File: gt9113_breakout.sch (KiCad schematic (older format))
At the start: 54 parts, among them J1 Conn_01x04_Male, J2 10118194-0001LF, J3 Conn_01x04_Male, J4 Conn_01x07_Male, J5 Conn_01x01_Male, J7 504740-5100, J8 504740-5100, Q1 2N7002E, U1 mXT2952TD, U2 HT7533-1-SOT89, Y1 DNF/16MHz

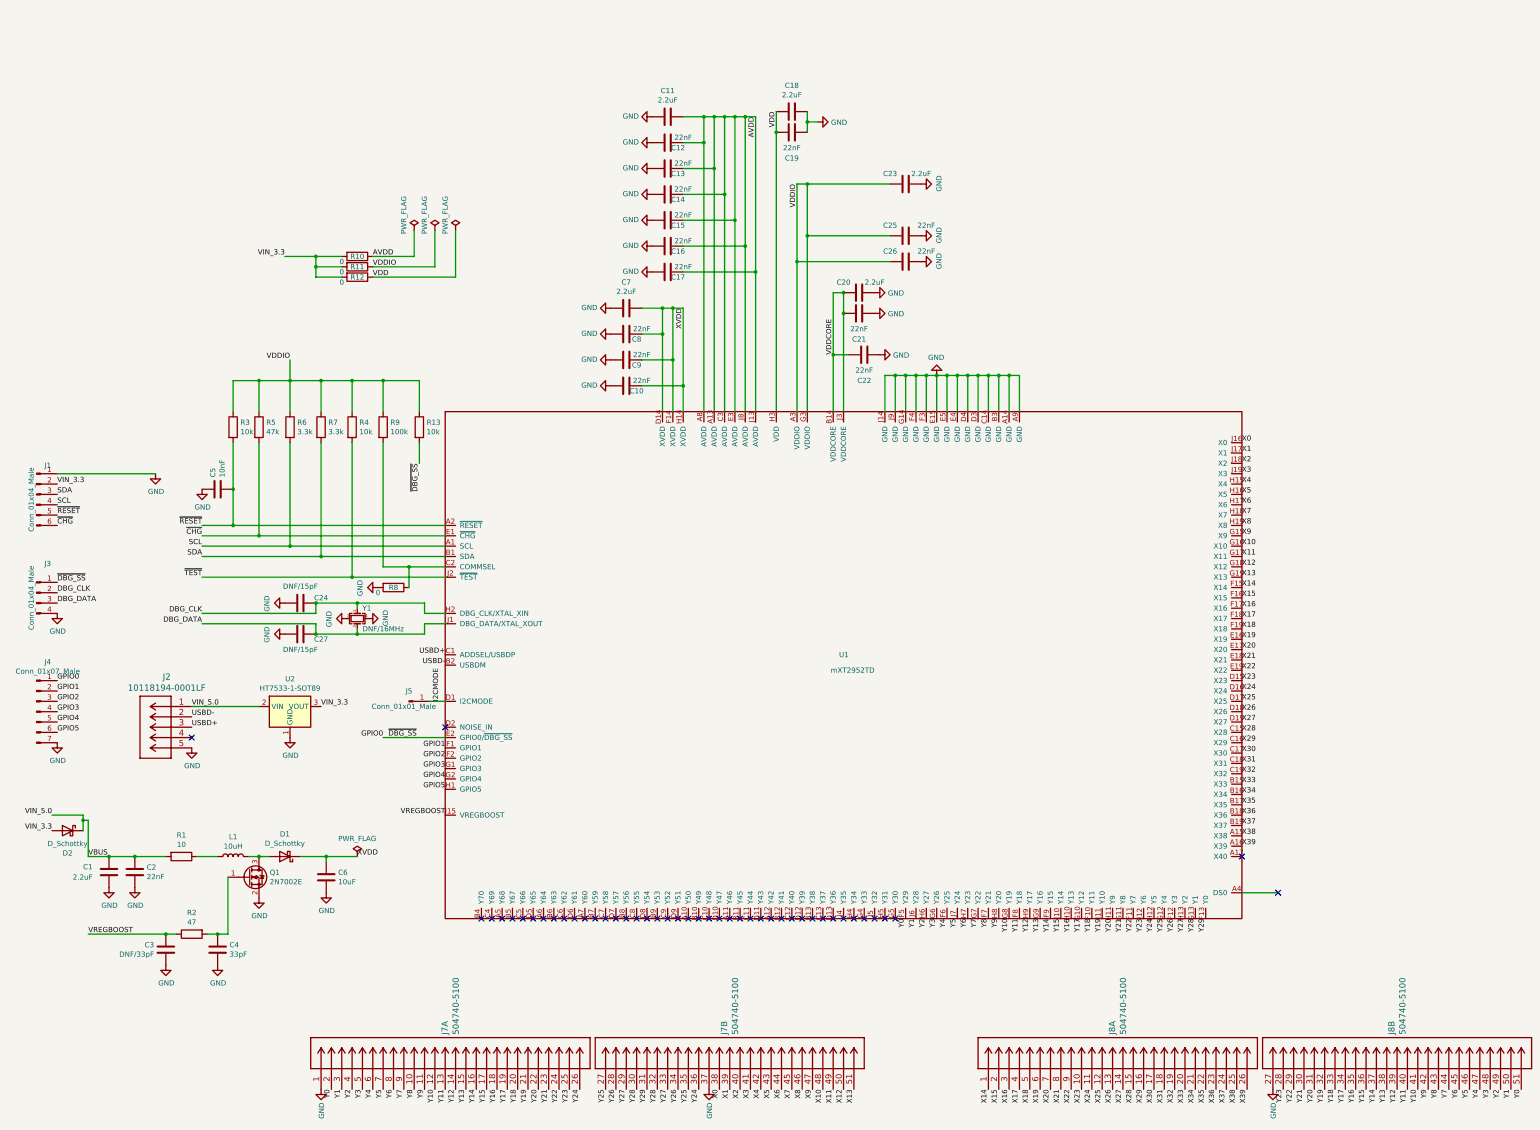
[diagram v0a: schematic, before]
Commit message: Remove all traces of atmxt2952. enable pth_and_npth_single_file since that's what jlcpcb wants
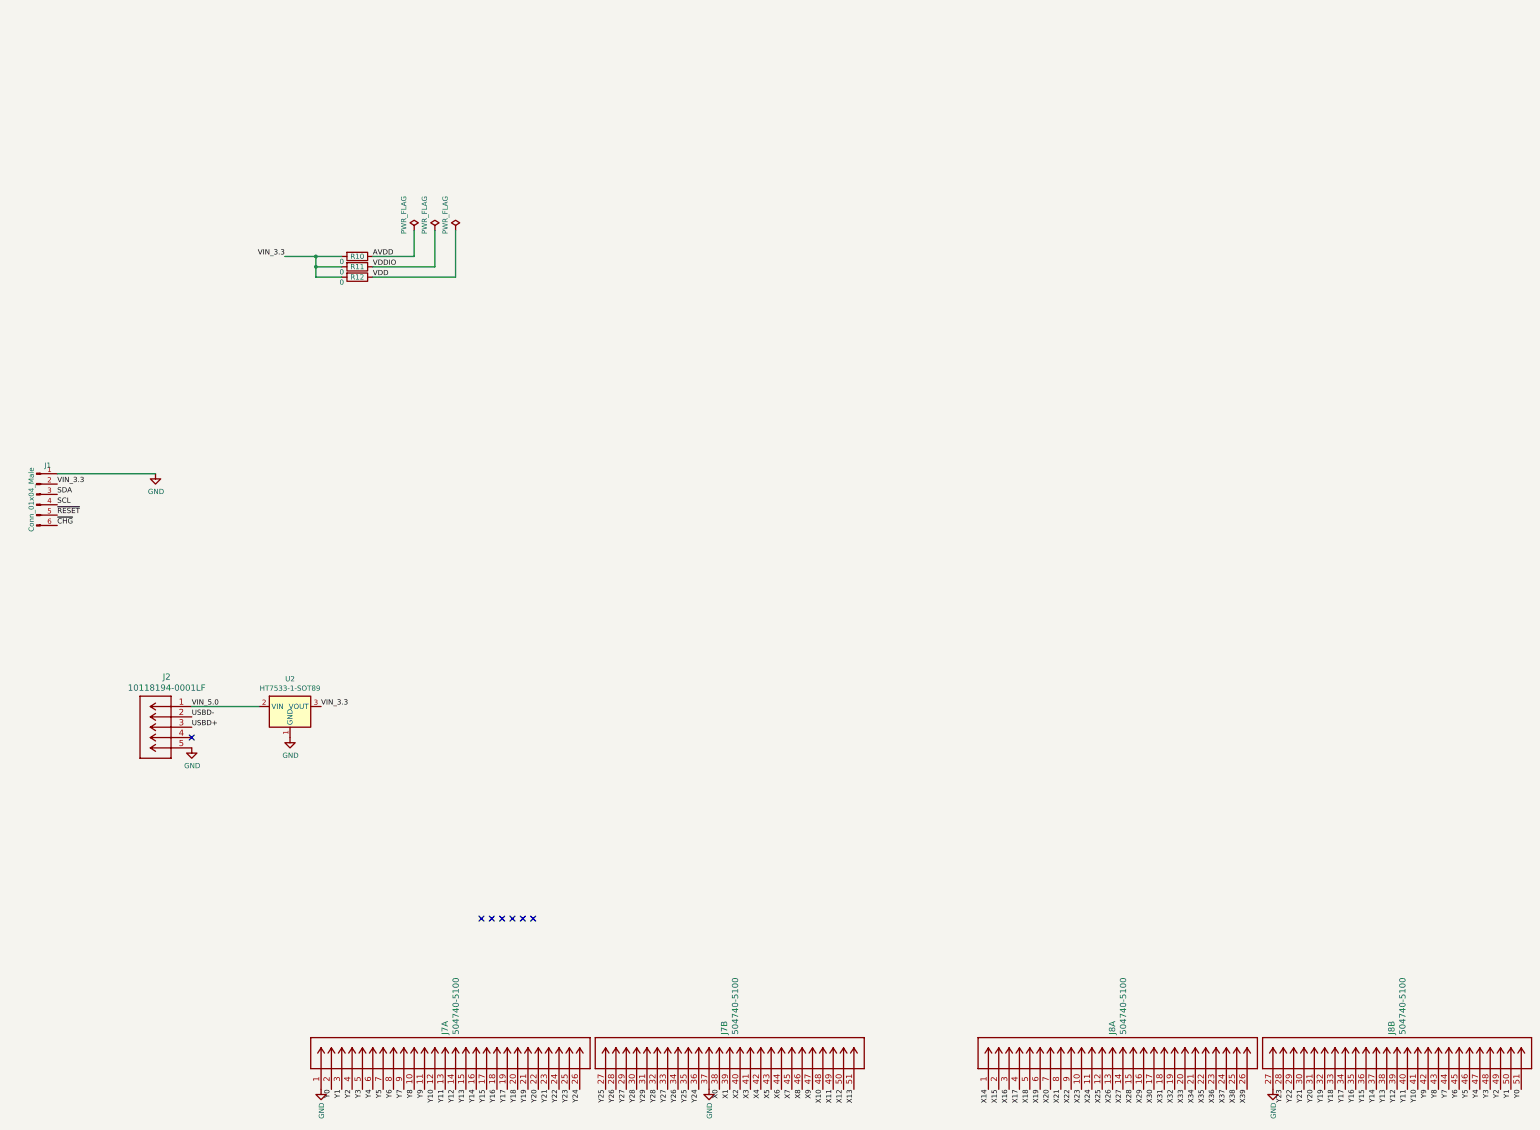
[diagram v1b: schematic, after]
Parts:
- removed C1, C11, C18, C20, C23, C7: 2.2uF, Capacitor_SMD:C_0603_1608Metric, symbol Device:C
- removed C10, C12, C13, C14, C15, C16, C17, C19, C2, C21, C22, C25, C26, C8, C9: 22nF, Capacitor_SMD:C_0402_1005Metric, symbol Device:C
- removed C24, C27: DNF/15pF, Capacitor_SMD:C_0603_1608Metric_Pad1.05x0.95mm_HandSolder, symbol Device:C
- removed C3: DNF/33pF, Capacitor_SMD:C_0603_1608Metric_Pad1.05x0.95mm_HandSolder, symbol Device:C
- removed C4: 33pF, Capacitor_SMD:C_0402_1005Metric, symbol Device:C
- removed C5: 10nF, Capacitor_SMD:C_0402_1005Metric, symbol Device:C
- removed C6: 10uF, Capacitor_SMD:C_0603_1608Metric, symbol Device:C
- removed D1, D2: D_Schottky, Diode_SMD:D_SOD-123, symbol Device:D_Schottky
- removed J3: Conn_01x04_Male, Connector_PinHeader_1.00mm:PinHeader_1x04_P1.00mm_Vertical, symbol Connector:Conn_01x04_Male
- removed J4: Conn_01x07_Male, Connector_PinHeader_1.00mm:PinHeader_1x07_P1.00mm_Vertical, symbol Connector:Conn_01x07_Male
- removed J5: Conn_01x01_Male, Connector_PinHeader_1.00mm:PinHeader_1x01_P1.00mm_Vertical, symbol Connector:Conn_01x01_Male
- removed L1: 10uH, Inductor_SMD:L_0603_1608Metric, symbol Device:L
- removed Q1: 2N7002E, Package_TO_SOT_SMD:SOT-23, symbol Transistor_FET:2N7002E
- removed R1: 10, Resistor_SMD:R_0402_1005Metric, symbol Device:R
- removed R13, R3, R4: 10k, Resistor_SMD:R_0402_1005Metric, symbol Device:R
- removed R2: 47, Resistor_SMD:R_0402_1005Metric, symbol Device:R
- removed R5: 47k, Resistor_SMD:R_0402_1005Metric, symbol Device:R
- removed R6, R7: 3.3k, Resistor_SMD:R_0402_1005Metric, symbol Device:R
- removed R8: 0, Resistor_SMD:R_0402_1005Metric, symbol Device:R
- removed R9: 100k, Resistor_SMD:R_0402_1005Metric, symbol Device:R
- removed U1: mXT2952TD, footprints:mXT2952TD, symbol atmxt2952td:mXT2952TD
- removed Y1: DNF/16MHz, Crystal:Crystal_SMD_3225-4Pin_3.2x2.5mm_HandSoldering, symbol Device:Crystal_GND24_Small
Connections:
- net VBUS renamed VIN_5.0
- no-connect marks 45 -> 7
